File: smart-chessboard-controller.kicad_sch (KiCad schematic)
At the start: 67 parts, among them J1 USB_C_Receptacle_USB2.0, J2 Micro_SD_Card_Det_Hirose_DM3C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, J3 Conn_02x03_Odd_Even, J4 Conn_01x12_MountingPin, J5 NX3224T024, J6 Conn_01x05, J7 Conn_01x05, J8 Conn_01x05, J9 Conn_01x05, Q1 S8050, Q2 S8050, SW1 SW_SPST, SW2 SW_SPST, SW3 SW_SPST, SW4 SW_SPST, U1 XC6220B331MR-G, U2 ESP32-WROOM-32E (8MB), U3 SP0503BAHT, U4 CP2102-GMR, U5 PCA9548APW, U6 TXS0102DCT

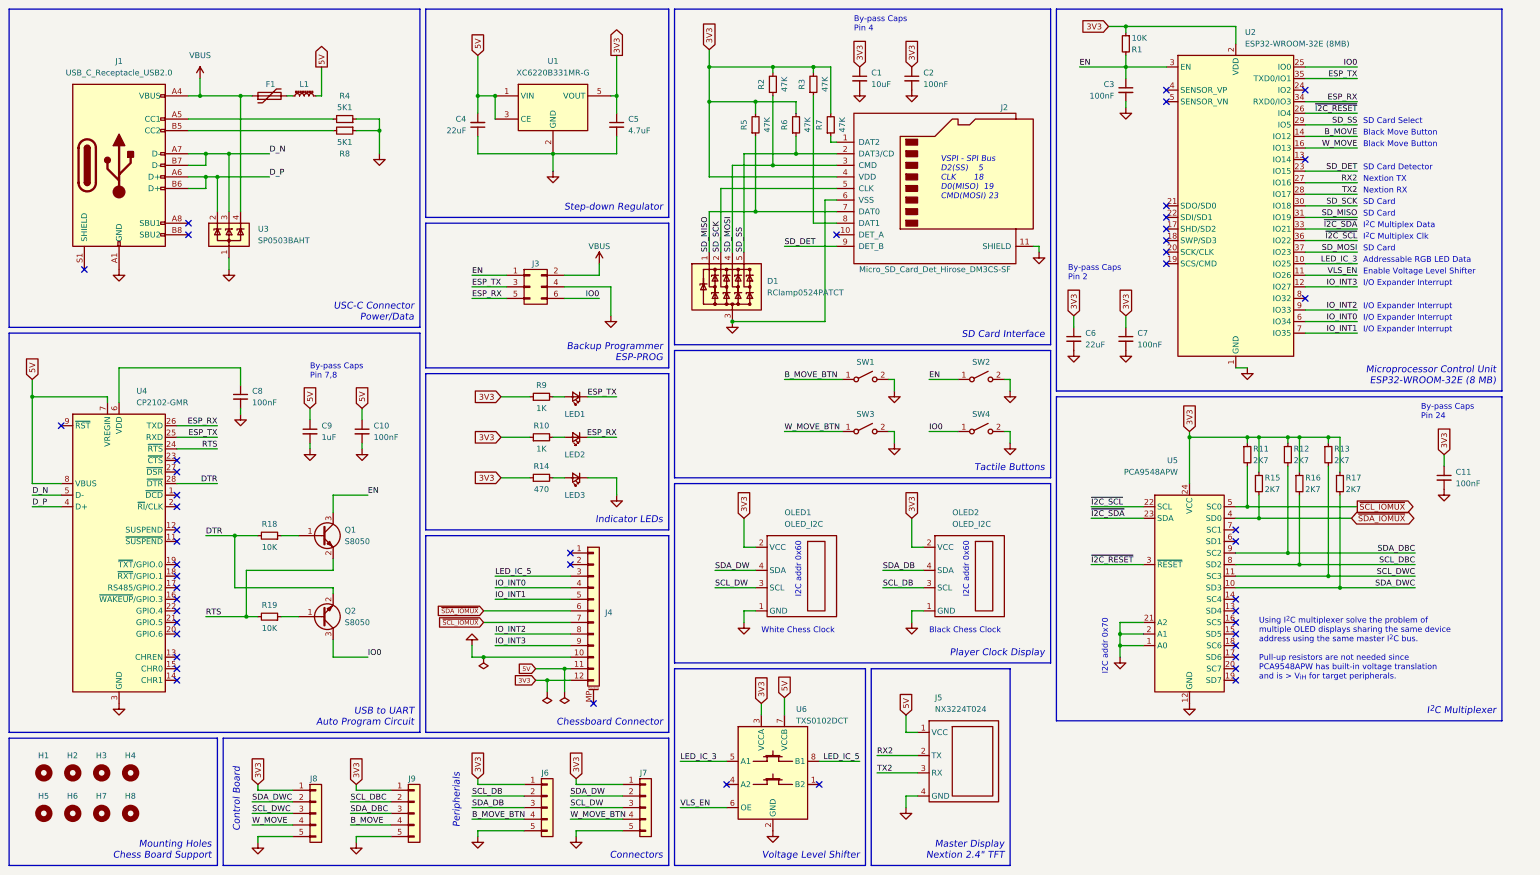
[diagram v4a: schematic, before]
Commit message: move usb-c to the side of the pcb
- revise ground nets for clock boards
- add backup led IC data line if the voltage regulator fails
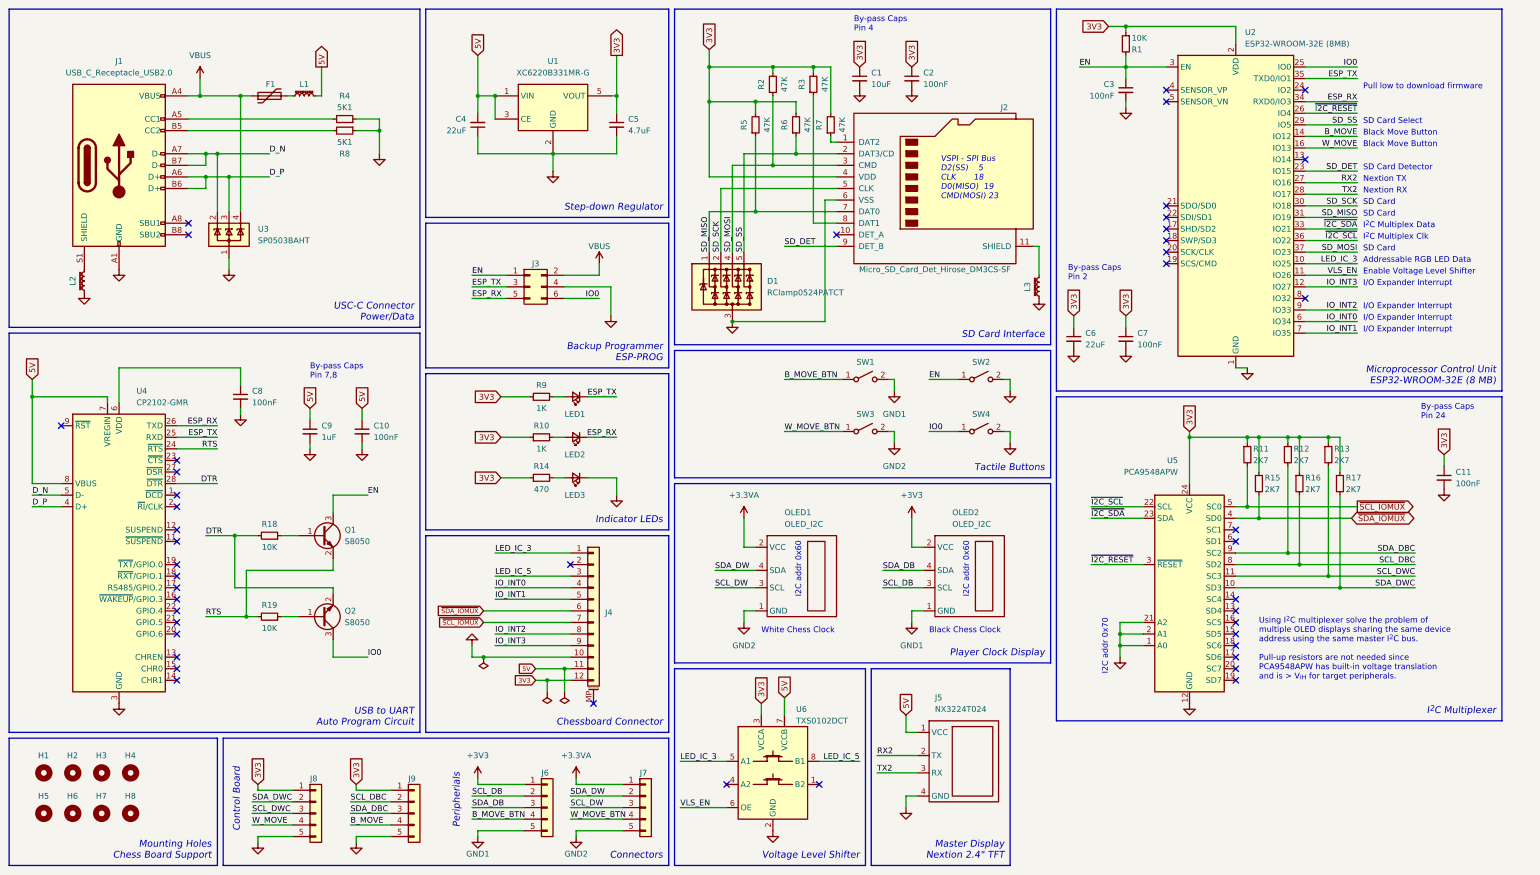
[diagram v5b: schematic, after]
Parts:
- added L2, L3: L_Ferrite_Small, Inductor_SMD:L_0603_1608Metric, symbol Device:L_Ferrite_Small
- J6, J7, J8, J9: now left out of the parts list
- U6: LCSC (none) -> C324082
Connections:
- net 3V3: no longer J6.1 (Pin_1), J7.1 (Pin_1), OLED1.2 (VCC), OLED2.2 (VCC)
- net D_N: now also U3.2 (K); no longer U3.3 (K)
- net D_P: now also U3.3 (K); no longer U3.2 (K)
- net GND: now also L2.1, L3.1; no longer J2.11 (SHIELD), J6.5 (Pin_5), J7.5 (Pin_5), OLED1.1 (GND), OLED2.1 (GND), SW1.2 (B), SW3.2 (B)
- net LED_IC_3: now also J4.1 (Pin_1)
- net at J1.S1 (SHIELD): now also L2.2
- new net: J2.11 (SHIELD), L3.2
- new net +3.3VA: J7.1 (Pin_1), OLED1.2 (VCC)
- new net +3V3: J6.1 (Pin_1), OLED2.2 (VCC)
- new net GND1: J6.5 (Pin_5), OLED2.1 (GND), SW1.2 (B)
- new net GND2: J7.5 (Pin_5), OLED1.1 (GND), SW3.2 (B)
- no-connect marks 47 -> 45
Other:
- note added: "Pull low to download firmware"

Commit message: fix pin assignment for black clock connector
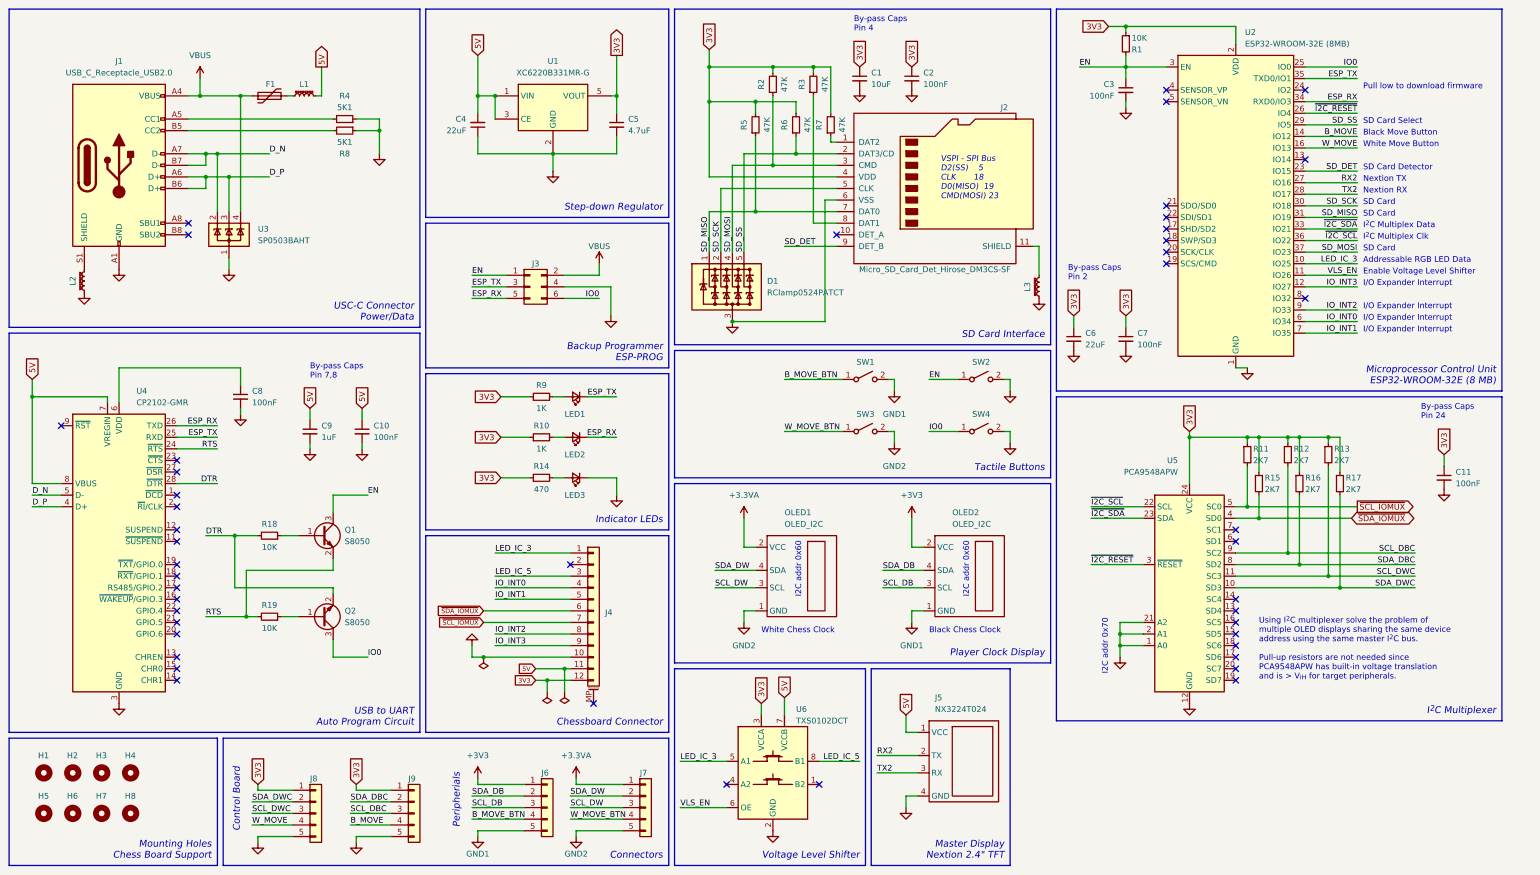
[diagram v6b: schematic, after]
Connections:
- net SCL_DB: now also J6.3 (Pin_3); no longer J6.2 (Pin_2)
- net SCL_DBC: now also J9.3 (Pin_3), R12.2, U5.9 (SC2); no longer J9.2 (Pin_2), R16.2, U5.8 (SD2)
- net SDA_DB: now also J6.2 (Pin_2); no longer J6.3 (Pin_3)
- net SDA_DBC: now also J9.2 (Pin_2), R16.2, U5.8 (SD2); no longer J9.3 (Pin_3), R12.2, U5.9 (SC2)
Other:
- note added: "White Move Button"
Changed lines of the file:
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@@
     (effects (font (size 1.5 1.5) italic) (justify right bottom))
   )
-  (text "Black Move Button" (at 311.15 44.45 0)
+  (text "White Move Button" (at 311.15 44.45 0)
     (effects (font (size 1.27 1.27)) (justify left bottom))
   )
@@
     (effects (font (size 1.27 1.27)) (justify right bottom))
   )
-  (label "SCL_DBC" (at 322.58 135.89 180)
+  (label "SCL_DBC" (at 322.58 133.35 180)
     (effects (font (size 1.27 1.27)) (justify right bottom))
   )
@@
     (effects (font (size 1.27 1.27)) (justify left bottom))
   )
-  (label "SCL_DBC" (at 88.9 187.96 0)
-    (effects (font (size 1.27 1.27)) (justify left bottom))
-  )
-  (label "SDA_DBC" (at 88.9 190.5 0)
+  (label "SCL_DBC" (at 88.9 190.5 0)
+    (effects (font (size 1.27 1.27)) (justify left bottom))
+  )
+  (label "SDA_DBC" (at 88.9 187.96 0)
     (effects (font (size 1.27 1.27)) (justify left bottom))
   )
@@
     (effects (font (size 1.27 1.27)) (justify left bottom))
   )
-  (label "SCL_DB" (at 115.57 186.69 0)
+  (label "SCL_DB" (at 115.57 189.23 0)
     (effects (font (size 1.27 1.27)) (justify left bottom))
   )
@@
     (effects (font (size 1.27 1.27)) (justify left bottom))
   )
-  (label "SDA_DBC" (at 322.58 133.35 180)
+  (label "SDA_DBC" (at 322.58 135.89 180)
     (effects (font (size 1.27 1.27)) (justify right bottom))
   )
@@
     (effects (font (size 1.27 1.27)) (justify right bottom))
   )
-  (label "SDA_DB" (at 115.57 189.23 0)
-    (effects (font (size 1.27 1.27)) (justify left bottom))
-  )
+  (label "SDA_DB" (at 115.57 186.69 0)
+    (effects (font (size 1.27 1.27)) (justify left bottom))
+  )

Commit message: remove chess clock/button
Remove chess clock/buttons from controller design. They were
moved to separate design since it's more expensive to
manufacture boards with panelization. They charge extra if
there are different designs with one gerber file with
panelization.
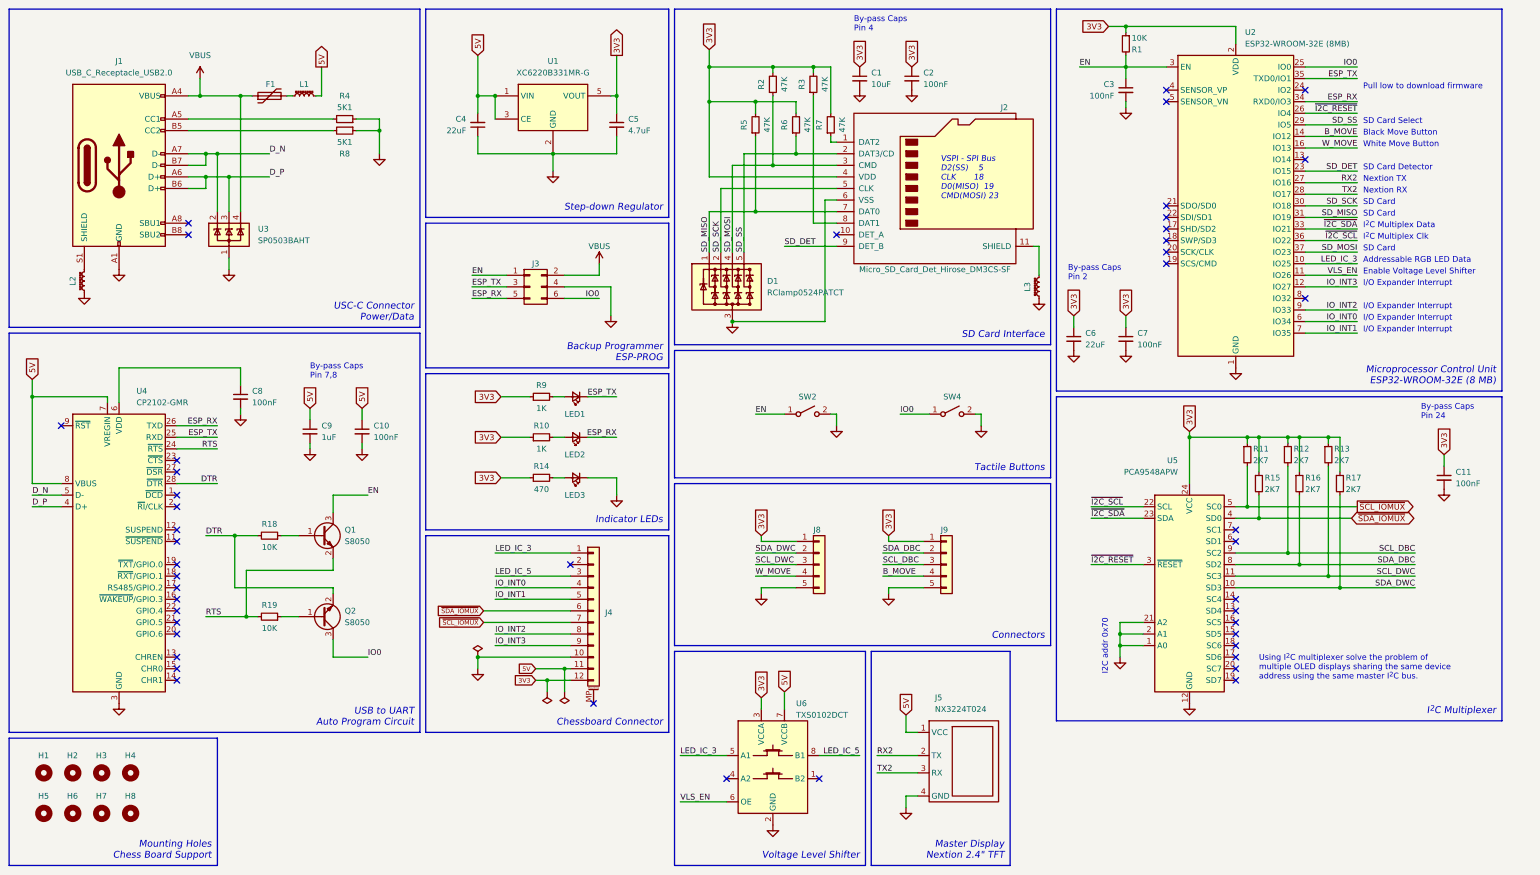
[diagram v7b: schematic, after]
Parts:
- removed J6, J7: Conn_01x05, Connector_JST:JST_PH_S5B-PH-K_1x05_P2.00mm_Horizontal, symbol Connector_Generic:Conn_01x05
- removed OLED1, OLED2: OLED_I2C, User Custom Footprint:OLED_128x32_I2C_4pins, symbol User_Symbols:OLED_I2C
- removed SW1, SW3: SW_SPST, User Custom Footprint:Button_SW_12mm_1.8mm_hole, symbol Switch:SW_SPST
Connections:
- net at J1.S1 (SHIELD), L2.2: now also J1.S2 (SHIELD), J1.S3 (SHIELD), J1.S4 (SHIELD)
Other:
- note added: "Using I^{2}C multiplexer solve the problem of multiple OLED displays sharing the same device address using the same master I^{2}C bus."
- note removed: "Black Chess Clock"
- note removed: "Control Board"
- note removed: "I2C addr 0x60"
- note removed: "Peripherials"
- note removed: "Player Clock Display"
- note removed: "Using I^{2}C multiplexer solve the problem of multiple OLED displays sharing the same device address using the same master I^{2}C bus. Pull-up resistors are not needed since PCA9548APW has built-in voltage translation and is > V_{iH} for target peripherals."
- note removed: "White Chess Clock"
- moved on the sheet: J8, J9, SW2, SW4, U6

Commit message: fix issues from rev.B
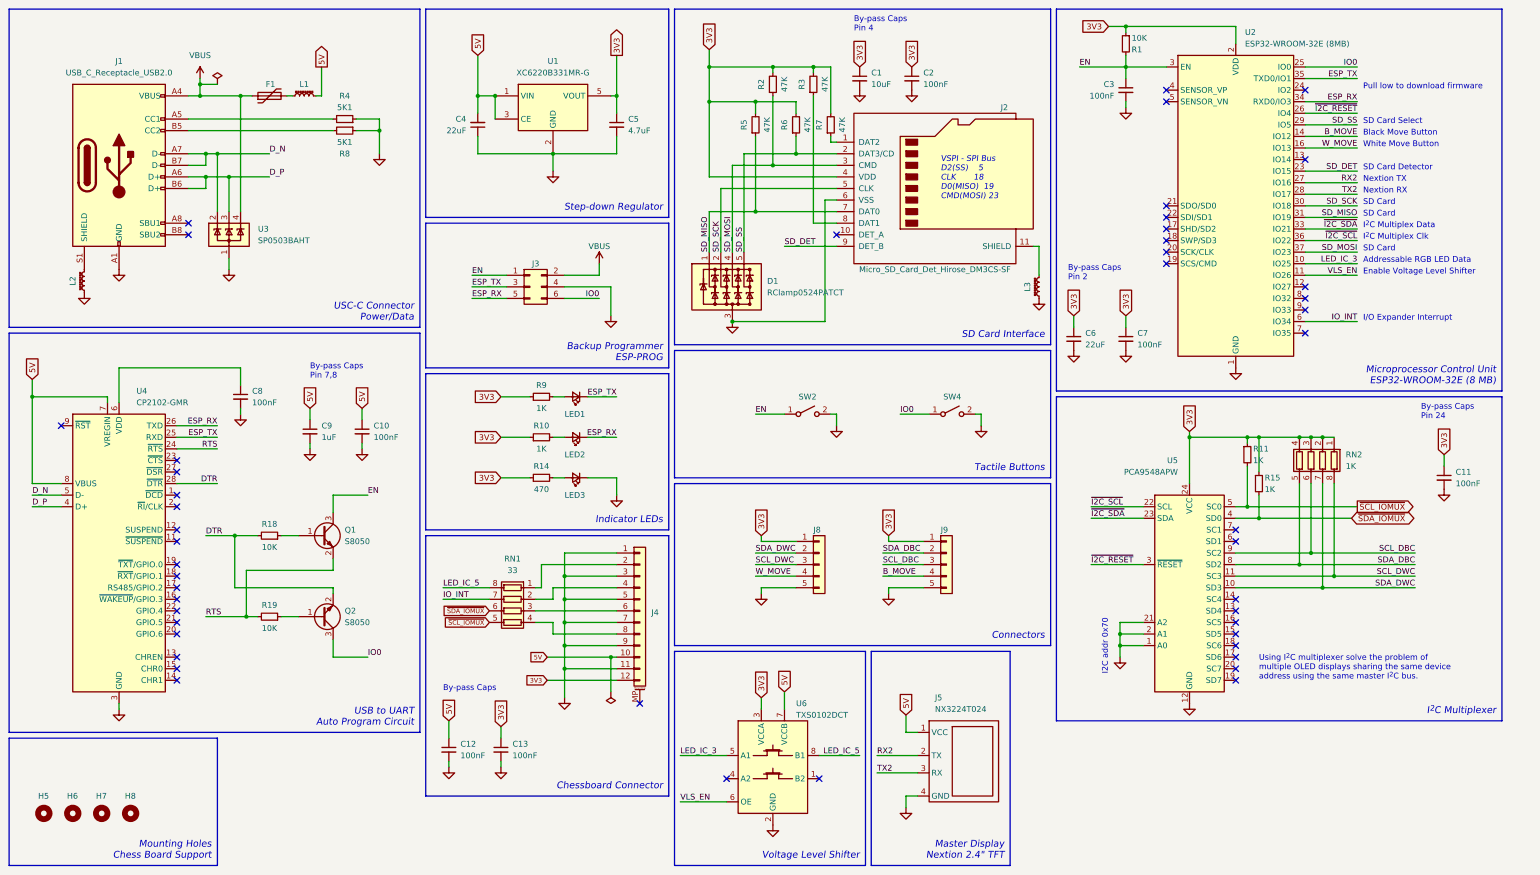
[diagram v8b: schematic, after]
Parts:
- removed H1, H2, H3, H4: MountingHole, MountingHole:MountingHole_2.7mm_M2.5_DIN965_Pad_TopBottom, symbol Mechanical:MountingHole
- removed R12, R13, R16, R17: 2K7, Resistor_SMD:R_0603_1608Metric, symbol Device:R_Small
- added C12, C13: 100nF, Capacitor_SMD:C_0603_1608Metric, symbol Device:C_Small
- added RN1: 33, Resistor_SMD:R_Array_Convex_4x0603, symbol Device:R_Pack04
- added RN2: 1K, Resistor_SMD:R_Array_Convex_4x0603, symbol Device:R_Pack04
- R11, R15: value 2K7 -> 1K; LCSC C13167 -> (none)
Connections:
- net 3V3: now also C13.1, RN2.1 (R1.1), RN2.2 (R2.1), RN2.3 (R3.1), RN2.4 (R4.1)
- net 5V: now also J4.10 (Pin_10), C12.1; no longer J4.11 (Pin_11)
- net GND: now also J4.1 (Pin_1), J4.11 (Pin_11), J4.3 (Pin_3), J4.5 (Pin_5), J4.7 (Pin_7), J4.9 (Pin_9), C12.2, C13.2; no longer J4.10 (Pin_10)
- net LED_IC_3: no longer J4.1 (Pin_1)
- net LED_IC_5: now also RN1.8 (R1.2); no longer J4.3 (Pin_3)
- net SCL_DBC: now also RN2.6 (R3.2)
- net SCL_DWC: now also RN2.8 (R1.2)
- net SDA_DBC: now also RN2.5 (R4.2)
- net SDA_DWC: now also RN2.7 (R2.2)
- net ~{SCL_IOMUX}: now also RN1.5 (R4.2); no longer J4.7 (Pin_7)
- net ~{SDA_IOMUX}: now also RN1.6 (R3.2); no longer J4.6 (Pin_6)
- net at J4.2 (Pin_2): now also RN1.1 (R1.1)
- net IO_INT0: no longer names the net of J4.4 (Pin_4)
- net IO_INT0: now also RN1.2 (R2.1); no longer U2.6 (IO34)
- net IO_INT1: no longer names the net of U2.7 (IO35)
- net IO_INT1: no longer J4.5 (Pin_5)
- net IO_INT2: no longer names the net of J4.8 (Pin_8)
- net IO_INT2: now also RN1.4 (R4.1); no longer U2.9 (IO33)
- net IO_INT3: no longer names the net of U2.12 (IO27)
- net IO_INT3: no longer J4.9 (Pin_9)
- new net: J4.6 (Pin_6), RN1.3 (R3.1)
- new net IO_INT: RN1.7 (R2.2), U2.6 (IO34)
- no-connect marks 45 -> 47
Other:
- note added: "By-pass Caps"
- moved on the sheet: J4
